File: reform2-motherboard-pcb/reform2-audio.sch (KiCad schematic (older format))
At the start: 52 parts, among them J16 LINE_IN, J21 Conn_01x04, J7 SJ-43516-SMT, U3 WM8960

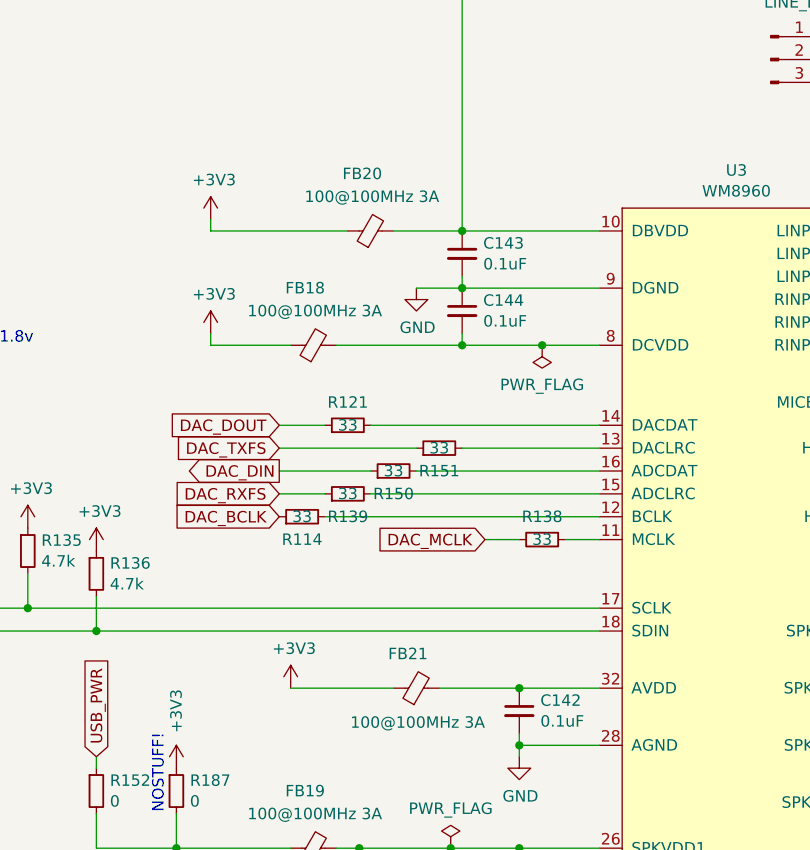
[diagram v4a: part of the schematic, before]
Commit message: reform2-motherboard: R-1 silkscreen cleanup; usb hub reset pulldown added
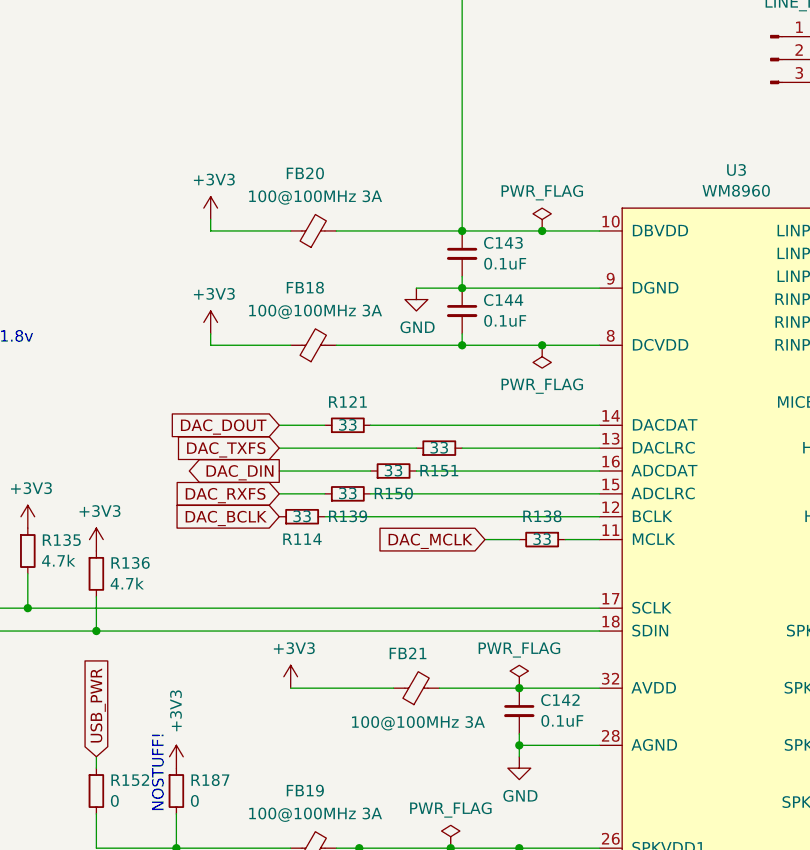
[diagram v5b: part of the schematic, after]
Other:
- moved on the sheet: FB20
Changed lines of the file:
@@
 	3050 2350 3050 2400
 Wire Wire Line
-	3050 2400 3650 2400
+	3050 2400 3400 2400
 $Comp
 L Device:C_Small C143
@@
 $EndComp
 Wire Wire Line
-	4150 2400 4750 2400
+	4150 2400 4500 2400
 Wire Wire Line
 	4750 2650 4150 2650
@@
 L Device:Ferrite_Bead_Small FB?
 U 1 1 601EEA4C
-P 3750 2400
+P 3500 2400
 AR Path="/5D06AC46/601EEA4C" Ref="FB?"  Part="1"
 AR Path="/5D1F6C04/601EEA4C" Ref="FB20"  Part="1"
-F 0 "FB20" V 4000 2350 50  0000 L CNN
-F 1 "100@100MHz 3A" V 3900 2100 50  0000 L CNN
-F 2 "Inductor_SMD:L_0603_1608Metric" V 3680 2400 50  0001 C CNN
-F 3 "~" H 3750 2400 50  0001 C CNN
-F 4 "Murata" H 3750 2400 50  0001 C CNN "Manufacturer"
-F 5 "BLM18KG101TN1D" H 3750 2400 50  0001 C CNN "Manufacturer_No"
-F 6 "y" H 3750 2400 50  0001 C CNN "Checked"
-F 7 "Mouser" H 3750 2400 50  0001 C CNN "Distributor"
-	1    3750 2400
-	0    -1   -1   0
-$EndComp
-Wire Wire Line
-	3850 2400 4150 2400
+F 0 "FB20" V 3750 2350 50  0000 L CNN
+F 1 "100@100MHz 3A" V 3650 2100 50  0000 L CNN
+F 2 "Inductor_SMD:L_0603_1608Metric" V 3430 2400 50  0001 C CNN
+F 3 "~" H 3500 2400 50  0001 C CNN
+F 4 "Murata" H 3500 2400 50  0001 C CNN "Manufacturer"
+F 5 "BLM18KG101TN1D" H 3500 2400 50  0001 C CNN "Manufacturer_No"
+F 6 "y" H 3500 2400 50  0001 C CNN "Checked"
+F 7 "Mouser" H 3500 2400 50  0001 C CNN "Distributor"
+	1    3500 2400
+	0    -1   -1   0
+$EndComp
+Wire Wire Line
+	3600 2400 4150 2400
 Connection ~ 4150 2400
 $Comp
@@
 Wire Wire Line
 	2550 4700 2550 4750
+$Comp
+L power:PWR_FLAG #FLG0121
+U 1 1 64A230F2
+P 4500 2400
+F 0 "#FLG0121" H 4500 2475 50  0001 C CNN
+F 1 "PWR_FLAG" H 4500 2573 50  0000 C CNN
+F 2 "" H 4500 2400 50  0001 C CNN
+F 3 "~" H 4500 2400 50  0001 C CNN
+	1    4500 2400
+	1    0    0    -1
+$EndComp
+Connection ~ 4500 2400
+Wire Wire Line
+	4500 2400 4750 2400
+$Comp
+L power:PWR_FLAG #FLG0122
+U 1 1 64A2504B
+P 4400 4400
+F 0 "#FLG0122" H 4400 4475 50  0001 C CNN
+F 1 "PWR_FLAG" H 4400 4573 50  0000 C CNN
+F 2 "" H 4400 4400 50  0001 C CNN
+F 3 "~" H 4400 4400 50  0001 C CNN
+	1    4400 4400
+	1    0    0    -1
+$EndComp
 $EndSCHEMATC

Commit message: motherboard: r-1 release snapshot
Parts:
- C141, C162, C163: Manufacturer_No UMK107AB7105KA-T -> UMK107BJ105KA-T
- C156, C158, C165, C166: Manufacturer (none) -> Yageo; Manufacturer_No (none) -> CC0603JPX7R9BB104
- C157, C159: Manufacturer (none) -> Taiyo Yuden; Manufacturer_No (none) -> TMK107B7474KA-TR
- D10: Distributor (none) -> Mouser; Manufacturer (none) -> Littelfuse; Manufacturer_No (none) -> SP0503BAHT
- R187: DNP (none) -> y
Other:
- note added: "NOSTUFF"
- note removed: "NOSTUFF!"
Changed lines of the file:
@@
 Sheet 2 9
 Title "Reform 2 Audio"
-Date "2020-05-19"
-Rev "2.0D-4"
+Date "2020-09-24"
+Rev "2.0R-1"
 Comp "MNT Research GmbH"
 Comment1 "https://mntre.com"
@@
 F 3 "~" H 6800 2600 50  0001 C CNN
 F 4 "Taiyo Yuden" H 6800 2600 50  0001 C CNN "Manufacturer"
-F 5 "UMK107AB7105KA-T" H 6800 2600 50  0001 C CNN "Manufacturer_No"
+F 5 "UMK107BJ105KA-T" H 6800 2600 50  0001 C CNN "Manufacturer_No"
 F 6 "y" H 6800 2600 50  0001 C CNN "Checked"
 F 7 "Mouser" H 6800 2600 50  0001 C CNN "Distributor"
@@
 F 6 "Vishay Dale" H 2900 4850 50  0001 C CNN "Manufacturer"
 F 7 "CRCW06030000Z0EAC" H 2900 4850 50  0001 C CNN "Manufacturer_No"
+F 8 "y" H 2900 4850 50  0001 C CNN "DNP"
 	1    2900 4850
 	1    0    0    -1
@@
 Connection ~ 4400 5800
 Text Notes 2850 4950 1    50   ~ 0
-NOSTUFF!
+NOSTUFF
 $Comp
 L power:PWR_FLAG #FLG0101
@@
 F 2 "Capacitor_SMD:C_0603_1608Metric" H 7450 4250 50  0001 C CNN
 F 3 "~" H 7450 4250 50  0001 C CNN
-F 4 "" H 7450 4250 50  0001 C CNN "Manufacturer"
-F 5 "" H 7450 4250 50  0001 C CNN "Manufacturer_No"
+F 4 "Taiyo Yuden" H 7450 4250 50  0001 C CNN "Manufacturer"
+F 5 "TMK107B7474KA-TR" H 7450 4250 50  0001 C CNN "Manufacturer_No"
 F 6 "" H 7450 4250 50  0001 C CNN "Checked"
 F 7 "Mouser" H 7450 4250 50  0001 C CNN "Distributor"
@@
 F 2 "Capacitor_SMD:C_0603_1608Metric" H 7450 4750 50  0001 C CNN
 F 3 "~" H 7450 4750 50  0001 C CNN
-F 4 "" H 7450 4750 50  0001 C CNN "Manufacturer"
-F 5 "" H 7450 4750 50  0001 C CNN "Manufacturer_No"
+F 4 "Taiyo Yuden" H 7450 4750 50  0001 C CNN "Manufacturer"
+F 5 "TMK107B7474KA-TR" H 7450 4750 50  0001 C CNN "Manufacturer_No"
 F 6 "" H 7450 4750 50  0001 C CNN "Checked"
 F 7 "Mouser" H 7450 4750 50  0001 C CNN "Distributor"
@@
 F 3 "~" H 5850 1750 50  0001 C CNN
 F 4 "Taiyo Yuden" H 5850 1750 50  0001 C CNN "Manufacturer"
-F 5 "UMK107AB7105KA-T" H 5850 1750 50  0001 C CNN "Manufacturer_No"
+F 5 "UMK107BJ105KA-T" H 5850 1750 50  0001 C CNN "Manufacturer_No"
 F 6 "y" H 5850 1750 50  0001 C CNN "Checked"
 F 7 "Mouser" H 5850 1750 50  0001 C CNN "Distributor"
@@
 F 3 "~" H 6100 1650 50  0001 C CNN
 F 4 "Taiyo Yuden" H 6100 1650 50  0001 C CNN "Manufacturer"
-F 5 "UMK107AB7105KA-T" H 6100 1650 50  0001 C CNN "Manufacturer_No"
+F 5 "UMK107BJ105KA-T" H 6100 1650 50  0001 C CNN "Manufacturer_No"
 F 6 "y" H 6100 1650 50  0001 C CNN "Checked"
 F 7 "Mouser" H 6100 1650 50  0001 C CNN "Distributor"
@@
 F 2 "Capacitor_SMD:C_0603_1608Metric" H 6800 4250 50  0001 C CNN
 F 3 "~" H 6800 4250 50  0001 C CNN
-F 4 "" H 6800 4250 50  0001 C CNN "Manufacturer"
-F 5 "" H 6800 4250 50  0001 C CNN "Manufacturer_No"
+F 4 "Yageo" H 6800 4250 50  0001 C CNN "Manufacturer"
+F 5 "CC0603JPX7R9BB104" H 6800 4250 50  0001 C CNN "Manufacturer_No"
 F 6 "" H 6800 4250 50  0001 C CNN "Checked"
 F 7 "Mouser" H 6800 4250 50  0001 C CNN "Distributor"
@@
 F 2 "Capacitor_SMD:C_0603_1608Metric" H 6900 4500 50  0001 C CNN
 F 3 "~" H 6900 4500 50  0001 C CNN
-F 4 "" H 6900 4500 50  0001 C CNN "Manufacturer"
-F 5 "" H 6900 4500 50  0001 C CNN "Manufacturer_No"
+F 4 "Yageo" H 6900 4500 50  0001 C CNN "Manufacturer"
+F 5 "CC0603JPX7R9BB104" H 6900 4500 50  0001 C CNN "Manufacturer_No"
 F 6 "" H 6900 4500 50  0001 C CNN "Checked"
 F 7 "Mouser" H 6900 4500 50  0001 C CNN "Distributor"
@@
 F 2 "Capacitor_SMD:C_0603_1608Metric" H 7000 4750 50  0001 C CNN
 F 3 "~" H 7000 4750 50  0001 C CNN
-F 4 "" H 7000 4750 50  0001 C CNN "Manufacturer"
-F 5 "" H 7000 4750 50  0001 C CNN "Manufacturer_No"
+F 4 "Yageo" H 7000 4750 50  0001 C CNN "Manufacturer"
+F 5 "CC0603JPX7R9BB104" H 7000 4750 50  0001 C CNN "Manufacturer_No"
 F 6 "" H 7000 4750 50  0001 C CNN "Checked"
 F 7 "Mouser" H 7000 4750 50  0001 C CNN "Distributor"
@@
 F 2 "Capacitor_SMD:C_0603_1608Metric" H 7100 5000 50  0001 C CNN
 F 3 "~" H 7100 5000 50  0001 C CNN
-F 4 "" H 7100 5000 50  0001 C CNN "Manufacturer"
-F 5 "" H 7100 5000 50  0001 C CNN "Manufacturer_No"
+F 4 "Yageo" H 7100 5000 50  0001 C CNN "Manufacturer"
+F 5 "CC0603JPX7R9BB104" H 7100 5000 50  0001 C CNN "Manufacturer_No"
 F 6 "" H 7100 5000 50  0001 C CNN "Checked"
 F 7 "Mouser" H 7100 5000 50  0001 C CNN "Distributor"
@@
 F 2 "Package_TO_SOT_SMD:SOT-143" H 8875 3900 50  0001 L CNN
 F 3 "http://www.littelfuse.com/~/media/files/littelfuse/technical%20resources/documents/data%20sheets/sp05xxba.pdf" H 8775 4075 50  0001 C CNN
+F 4 "Mouser" H 8650 3950 50  0001 C CNN "Distributor"
+F 5 "Littelfuse" H 8650 3950 50  0001 C CNN "Manufacturer"
+F 6 "SP0503BAHT" H 8650 3950 50  0001 C CNN "Manufacturer_No"
 	1    8650 3950
 	1    0    0    -1

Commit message: reform2-motherboard: schematics,PCB,BOM,models for R-2C (probably final)
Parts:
- added C170: 4.7uF, Capacitor_SMD:C_0603_1608Metric, symbol Device:C_Small
- C156, C157, C158, C159, C165, C166, D10, J16, L10, L11, L8, L9: Checked (none) -> y
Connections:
- net GND: now also C170.2
- net at R140.1, U3.1 (MICBIAS): now also C170.1
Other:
- note removed: "NOTE: ref1 used 0.1uF and 2k2"
- note removed: "TODO: actually test 5v"
- moved on the sheet: C127, C141, C147, R140
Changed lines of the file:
@@
 Sheet 2 9
 Title "Reform 2 Audio"
-Date "2020-09-24"
-Rev "2.0R-1"
+Date "2020-10-29"
+Rev "2.0R-2C"
 Comp "MNT Research GmbH"
 Comment1 "https://mntre.com"
@@
 Connection ~ 4400 6050
 Wire Wire Line
-	6200 3650 5950 3650
-Wire Wire Line
-	6400 3650 6650 3650
-Wire Wire Line
-	6600 3350 6950 3350
-Wire Wire Line
-	6400 3350 5950 3350
+	6150 3650 5950 3650
+Wire Wire Line
+	6350 3650 6650 3650
+Wire Wire Line
+	6350 3350 6950 3350
+Wire Wire Line
+	6150 3350 5950 3350
 $Comp
 L Device:R_Small R143
@@
 	6950 3850 6650 3850
 Wire Wire Line
-	6050 3150 5950 3150
+	6900 3150 6450 3150
 Wire Wire Line
 	7250 3250 8900 3250
@@
 L Device:C_Small C147
 U 1 1 5F2211CD
-P 6500 3350
-F 0 "C147" V 6550 3200 50  0000 C CNN
-F 1 "47uF" V 6600 3350 50  0000 C CNN
-F 2 "Capacitor_SMD:C_0603_1608Metric" H 6500 3350 50  0001 C CNN
-F 3 "~" H 6500 3350 50  0001 C CNN
-F 4 "Murata" H 6500 3350 50  0001 C CNN "Manufacturer"
-F 5 "GRM188R60J476ME15D" H 6500 3350 50  0001 C CNN "Manufacturer_No"
-F 6 "y" H 6500 3350 50  0001 C CNN "Checked"
-F 7 "Mouser" H 6500 3350 50  0001 C CNN "Distributor"
-	1    6500 3350
+P 6250 3350
+F 0 "C147" V 6300 3200 50  0000 C CNN
+F 1 "47uF" V 6350 3350 50  0000 C CNN
+F 2 "Capacitor_SMD:C_0603_1608Metric" H 6250 3350 50  0001 C CNN
+F 3 "~" H 6250 3350 50  0001 C CNN
+F 4 "Murata" H 6250 3350 50  0001 C CNN "Manufacturer"
+F 5 "GRM188R60J476ME15D" H 6250 3350 50  0001 C CNN "Manufacturer_No"
+F 6 "y" H 6250 3350 50  0001 C CNN "Checked"
+F 7 "Mouser" H 6250 3350 50  0001 C CNN "Distributor"
+	1    6250 3350
 	0    1    1    0
 $EndComp
@@
 L Device:C_Small C127
 U 1 1 5F2217E7
-P 6300 3650
-F 0 "C127" V 6350 3500 50  0000 C CNN
-F 1 "47uF" V 6400 3650 50  0000 C CNN
-F 2 "Capacitor_SMD:C_0603_1608Metric" H 6300 3650 50  0001 C CNN
-F 3 "~" H 6300 3650 50  0001 C CNN
-F 4 "Murata" H 6300 3650 50  0001 C CNN "Manufacturer"
-F 5 "GRM188R60J476ME15D" H 6300 3650 50  0001 C CNN "Manufacturer_No"
-F 6 "y" H 6300 3650 50  0001 C CNN "Checked"
-F 7 "Mouser" H 6300 3650 50  0001 C CNN "Distributor"
-	1    6300 3650
+P 6250 3650
+F 0 "C127" V 6300 3500 50  0000 C CNN
+F 1 "47uF" V 6350 3650 50  0000 C CNN
+F 2 "Capacitor_SMD:C_0603_1608Metric" H 6250 3650 50  0001 C CNN
+F 3 "~" H 6250 3650 50  0001 C CNN
+F 4 "Murata" H 6250 3650 50  0001 C CNN "Manufacturer"
+F 5 "GRM188R60J476ME15D" H 6250 3650 50  0001 C CNN "Manufacturer_No"
+F 6 "y" H 6250 3650 50  0001 C CNN "Checked"
+F 7 "Mouser" H 6250 3650 50  0001 C CNN "Distributor"
+	1    6250 3650
 	0    1    1    0
 $EndComp
@@
 F 3 "~" H 5500 1650 50  0001 C CNN
 F 4 "y" H 5500 1650 50  0001 C CNN "DNP"
+F 5 "y" H 5500 1650 50  0001 C CNN "Checked"
 	1    5500 1650
 	1    0    0    -1
@@
 $EndComp
 Wire Wire Line
-	6250 3150 7250 3150
+	7100 3150 7250 3150
 Wire Wire Line
 	7950 4150 7950 4450
@@
 L Device:C_Small C141
 U 1 1 6830926E
-P 6800 2600
-F 0 "C141" H 6892 2646 50  0000 L CNN
-F 1 "1uF" H 6892 2555 50  0000 L CNN
-F 2 "Capacitor_SMD:C_0603_1608Metric" H 6800 2600 50  0001 C CNN
-F 3 "~" H 6800 2600 50  0001 C CNN
-F 4 "Taiyo Yuden" H 6800 2600 50  0001 C CNN "Manufacturer"
-F 5 "UMK107BJ105KA-T" H 6800 2600 50  0001 C CNN "Manufacturer_No"
-F 6 "y" H 6800 2600 50  0001 C CNN "Checked"
-F 7 "Mouser" H 6800 2600 50  0001 C CNN "Distributor"
-	1    6800 2600
+P 7100 2600
+F 0 "C141" H 7192 2646 50  0000 L CNN
+F 1 "1uF" H 7192 2555 50  0000 L CNN
+F 2 "Capacitor_SMD:C_0603_1608Metric" H 7100 2600 50  0001 C CNN
+F 3 "~" H 7100 2600 50  0001 C CNN
+F 4 "Taiyo Yuden" H 7100 2600 50  0001 C CNN "Manufacturer"
+F 5 "UMK107BJ105KA-T" H 7100 2600 50  0001 C CNN "Manufacturer_No"
+F 6 "y" H 7100 2600 50  0001 C CNN "Checked"
+F 7 "Mouser" H 7100 2600 50  0001 C CNN "Distributor"
+	1    7100 2600
 	0    1    1    0
 $EndComp
 Wire Wire Line
-	5950 2600 6700 2600
-Wire Wire Line
-	6900 2600 7250 2600
+	5950 2600 7000 2600
+Wire Wire Line
+	7200 2600 7250 2600
 Wire Wire Line
 	7250 2600 7250 3150
@@
 L Device:R_Small R140
 U 1 1 5F0E8F60
-P 6150 3150
-F 0 "R140" V 6250 3150 50  0000 C CNN
-F 1 "680" V 6050 3150 50  0000 C CNN
-F 2 "Resistor_SMD:R_0603_1608Metric" H 6150 3150 50  0001 C CNN
-F 3 "~" H 6150 3150 50  0001 C CNN
-F 4 "Yageo" H 6150 3150 50  0001 C CNN "Manufacturer"
-F 5 "RC0603FR-07680RL" H 6150 3150 50  0001 C CNN "Manufacturer_No"
-F 6 "Mouser" H 6150 3150 50  0001 C CNN "Distributor"
-F 7 "y" H 6150 3150 50  0001 C CNN "Checked"
-	1    6150 3150
+P 7000 3150
+F 0 "R140" V 7100 3150 50  0000 C CNN
+F 1 "680" V 6900 3150 50  0000 C CNN
+F 2 "Resistor_SMD:R_0603_1608Metric" H 7000 3150 50  0001 C CNN
+F 3 "~" H 7000 3150 50  0001 C CNN
+F 4 "Yageo" H 7000 3150 50  0001 C CNN "Manufacturer"
+F 5 "RC0603FR-07680RL" H 7000 3150 50  0001 C CNN "Manufacturer_No"
+F 6 "Mouser" H 7000 3150 50  0001 C CNN "Distributor"
+F 7 "y" H 7000 3150 50  0001 C CNN "Checked"
+	1    7000 3150
 	0    -1   -1   0
 $EndComp
@@
 F 4 "Taiyo Yuden" H 7450 4250 50  0001 C CNN "Manufacturer"
 F 5 "TMK107B7474KA-TR" H 7450 4250 50  0001 C CNN "Manufacturer_No"
-F 6 "" H 7450 4250 50  0001 C CNN "Checked"
+F 6 "y" H 7450 4250 50  0001 C CNN "Checked"
 F 7 "Mouser" H 7450 4250 50  0001 C CNN "Distributor"
 	1    7450 4250
@@
 F 4 "Taiyo Yuden" H 7450 4750 50  0001 C CNN "Manufacturer"
 F 5 "TMK107B7474KA-TR" H 7450 4750 50  0001 C CNN "Manufacturer_No"
-F 6 "" H 7450 4750 50  0001 C CNN "Checked"
+F 6 "y" H 7450 4750 50  0001 C CNN "Checked"
 F 7 "Mouser" H 7450 4750 50  0001 C CNN "Distributor"
 	1    7450 4750
@@
 Text Notes 8050 5650 0    50   ~ 0
 alternative:\n47uF in series for lowpass
-Text Notes 2100 5300 0    50   ~ 0
-TODO: actually test 5v
 $Comp
 L Device:C_Small C162
@@
 Wire Wire Line
 	6000 1650 5700 1650
-Text Notes 5950 3000 0    50   ~ 0
-NOTE: ref1 used 0.1uF and 2k2
 Wire Wire Line
 	3050 2900 3050 2850
@@
 F 5 "Murata" H 6600 4650 50  0001 C CNN "Manufacturer"
 F 6 "LQH32PB150MN0L" H 6600 4650 50  0001 C CNN "Manufacturer_No"
+F 7 "y" H 6600 4650 50  0001 C CNN "Checked"
 	1    6600 4650
 	0    -1   -1   0
@@
 F 5 "Murata" H 6600 4400 50  0001 C CNN "Manufacturer"
 F 6 "LQH32PB150MN0L" H 6600 4400 50  0001 C CNN "Manufacturer_No"
+F 7 "y" H 6600 4400 50  0001 C CNN "Checked"
 	1    6600 4400
 	0    -1   -1   0
@@
 F 5 "Murata" H 6600 4900 50  0001 C CNN "Manufacturer"
 F 6 "LQH32PB150MN0L" H 6600 4900 50  0001 C CNN "Manufacturer_No"
+F 7 "y" H 6600 4900 50  0001 C CNN "Checked"
 	1    6600 4900
 	0    -1   -1   0
@@
 F 4 "Yageo" H 6800 4250 50  0001 C CNN "Manufacturer"
 F 5 "CC0603JPX7R9BB104" H 6800 4250 50  0001 C CNN "Manufacturer_No"
-F 6 "" H 6800 4250 50  0001 C CNN "Checked"
+F 6 "y" H 6800 4250 50  0001 C CNN "Checked"
 F 7 "Mouser" H 6800 4250 50  0001 C CNN "Distributor"
 	1    6800 4250
@@
 F 4 "Yageo" H 6900 4500 50  0001 C CNN "Manufacturer"
 F 5 "CC0603JPX7R9BB104" H 6900 4500 50  0001 C CNN "Manufacturer_No"
-F 6 "" H 6900 4500 50  0001 C CNN "Checked"
+F 6 "y" H 6900 4500 50  0001 C CNN "Checked"
 F 7 "Mouser" H 6900 4500 50  0001 C CNN "Distributor"
 	1    6900 4500
@@
 F 4 "Yageo" H 7000 4750 50  0001 C CNN "Manufacturer"
 F 5 "CC0603JPX7R9BB104" H 7000 4750 50  0001 C CNN "Manufacturer_No"
-F 6 "" H 7000 4750 50  0001 C CNN "Checked"
+F 6 "y" H 7000 4750 50  0001 C CNN "Checked"
 F 7 "Mouser" H 7000 4750 50  0001 C CNN "Distributor"
 	1    7000 4750
@@
 F 4 "Yageo" H 7100 5000 50  0001 C CNN "Manufacturer"
 F 5 "CC0603JPX7R9BB104" H 7100 5000 50  0001 C CNN "Manufacturer_No"
-F 6 "" H 7100 5000 50  0001 C CNN "Checked"
+F 6 "y" H 7100 5000 50  0001 C CNN "Checked"
 F 7 "Mouser" H 7100 5000 50  0001 C CNN "Distributor"
 	1    7100 5000
@@
 F 5 "Murata" H 6600 4150 50  0001 C CNN "Manufacturer"
 F 6 "LQH32PB150MN0L" H 6600 4150 50  0001 C CNN "Manufacturer_No"
+F 7 "y" H 6600 4150 50  0001 C CNN "Checked"
 	1    6600 4150
 	0    -1   -1   0
 $EndComp
-Text Notes 6300 4000 0    50   ~ 0
+Text Notes 6700 4050 0    50   ~ 0
 800mA
 $Comp
@@
 F 5 "Littelfuse" H 8650 3950 50  0001 C CNN "Manufacturer"
 F 6 "SP0503BAHT" H 8650 3950 50  0001 C CNN "Manufacturer_No"
+F 7 "y" H 8650 3950 50  0001 C CNN "Checked"
 	1    8650 3950
 	1    0    0    -1
@@
 	1    0    0    -1
 $EndComp
+$Comp
+L Device:C_Small C170
+U 1 1 5FA4DDEA
+P 6600 2850
+F 0 "C170" V 6650 2900 50  0000 L CNN
+F 1 "4.7uF" V 6650 2600 50  0000 L CNN
+F 2 "Capacitor_SMD:C_0603_1608Metric" H 6600 2850 50  0001 C CNN
+F 3 "~" H 6600 2850 50  0001 C CNN
+F 4 "TDK" H 6600 2850 50  0001 C CNN "Manufacturer"
+F 5 "C1608X5R1V475K080AC" H 6600 2850 50  0001 C CNN "Manufacturer_No"
+F 6 "y" H 6600 2850 50  0001 C CNN "Checked"
+F 7 "Mouser" H 6600 2850 50  0001 C CNN "Distributor"
+	1    6600 2850
+	0    -1   -1   0
+$EndComp
+$Comp
+L power:GND #PWR0125
+U 1 1 5FA55570
+P 6750 2900
+F 0 "#PWR0125" H 6750 2650 50  0001 C CNN
+F 1 "GND" H 6755 2727 50  0000 C CNN
+F 2 "" H 6750 2900 50  0001 C CNN
+F 3 "" H 6750 2900 50  0001 C CNN
+	1    6750 2900
+	1    0    0    -1
+$EndComp
+Connection ~ 6450 3150
+Wire Wire Line
+	6450 3150 5950 3150
+Wire Wire Line
+	6750 2900 6750 2850
+Wire Wire Line
+	6750 2850 6700 2850
+Wire Wire Line
+	6450 2850 6500 2850
+Wire Wire Line
+	6450 2850 6450 3150
 $EndSCHEMATC

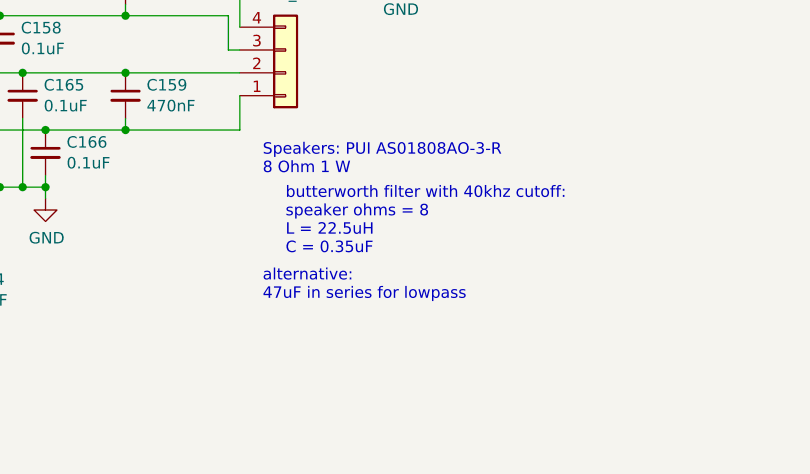
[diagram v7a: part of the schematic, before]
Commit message: reform2-motherboard: add pdf schematics
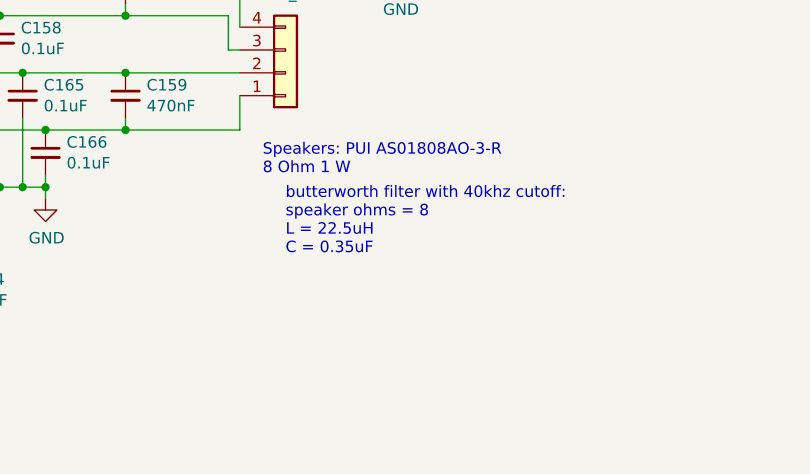
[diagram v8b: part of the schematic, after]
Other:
- note removed: "alternative:\n47uF in series for lowpass"
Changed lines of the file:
@@
 Wire Wire Line
 	4500 2900 4150 2900
-Text Notes 8050 5650 0    50   ~ 0
-alternative:\n47uF in series for lowpass
 $Comp
 L Device:C_Small C162
